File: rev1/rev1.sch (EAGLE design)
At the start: 26 parts, among them IC1 ATMEGA168-AU, Q1 MOSFET-NCHANNEL-IRLR3705ZPBF, Y1 16MHz

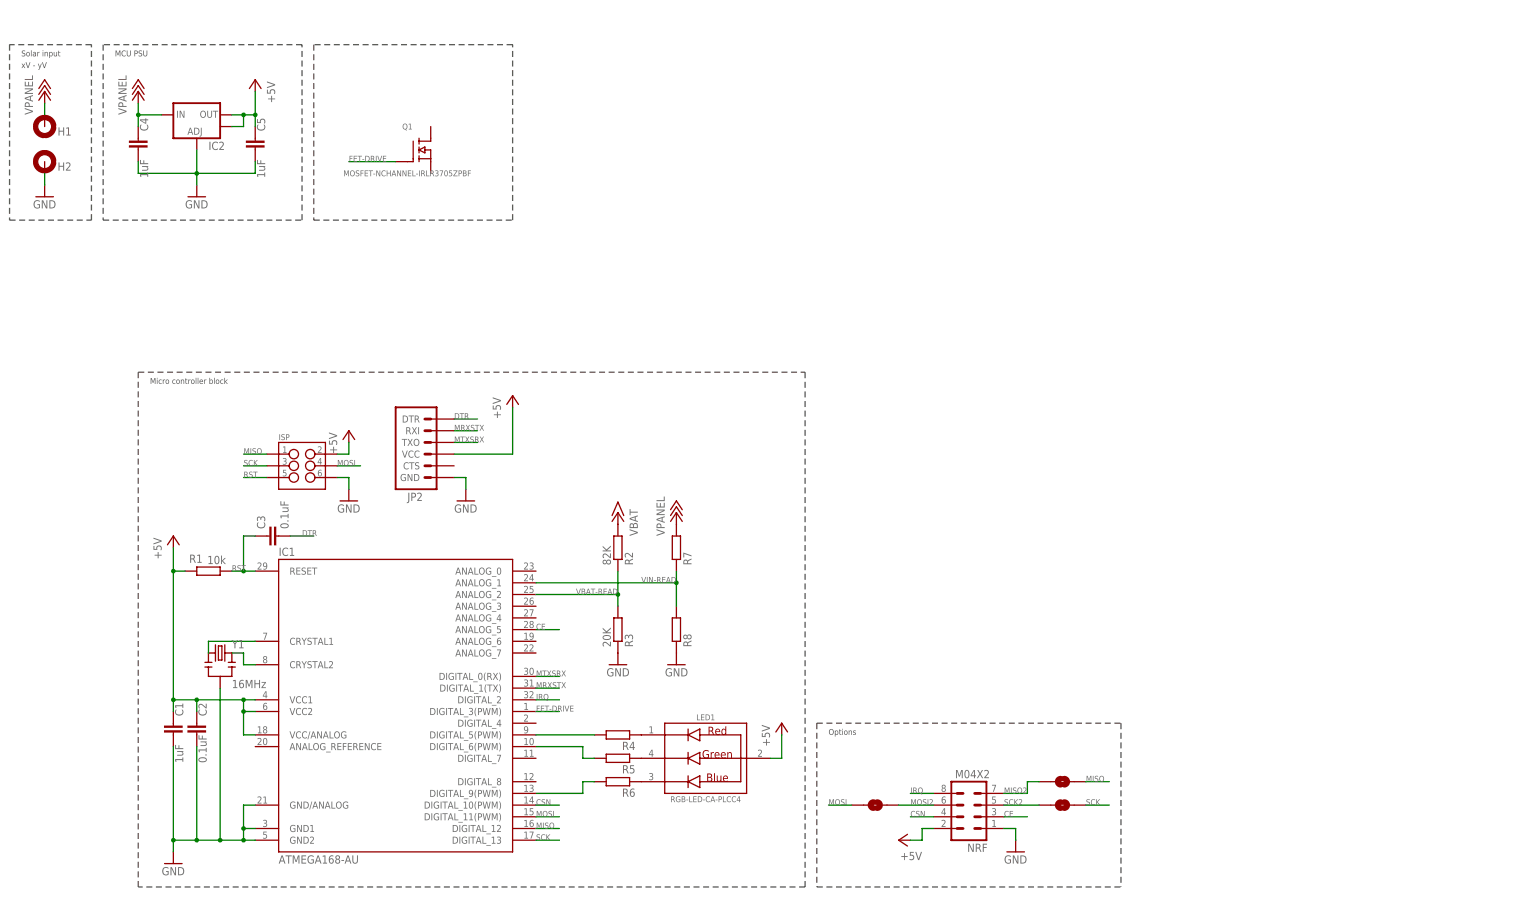
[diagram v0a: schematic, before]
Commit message: Added charge pump for v-gate
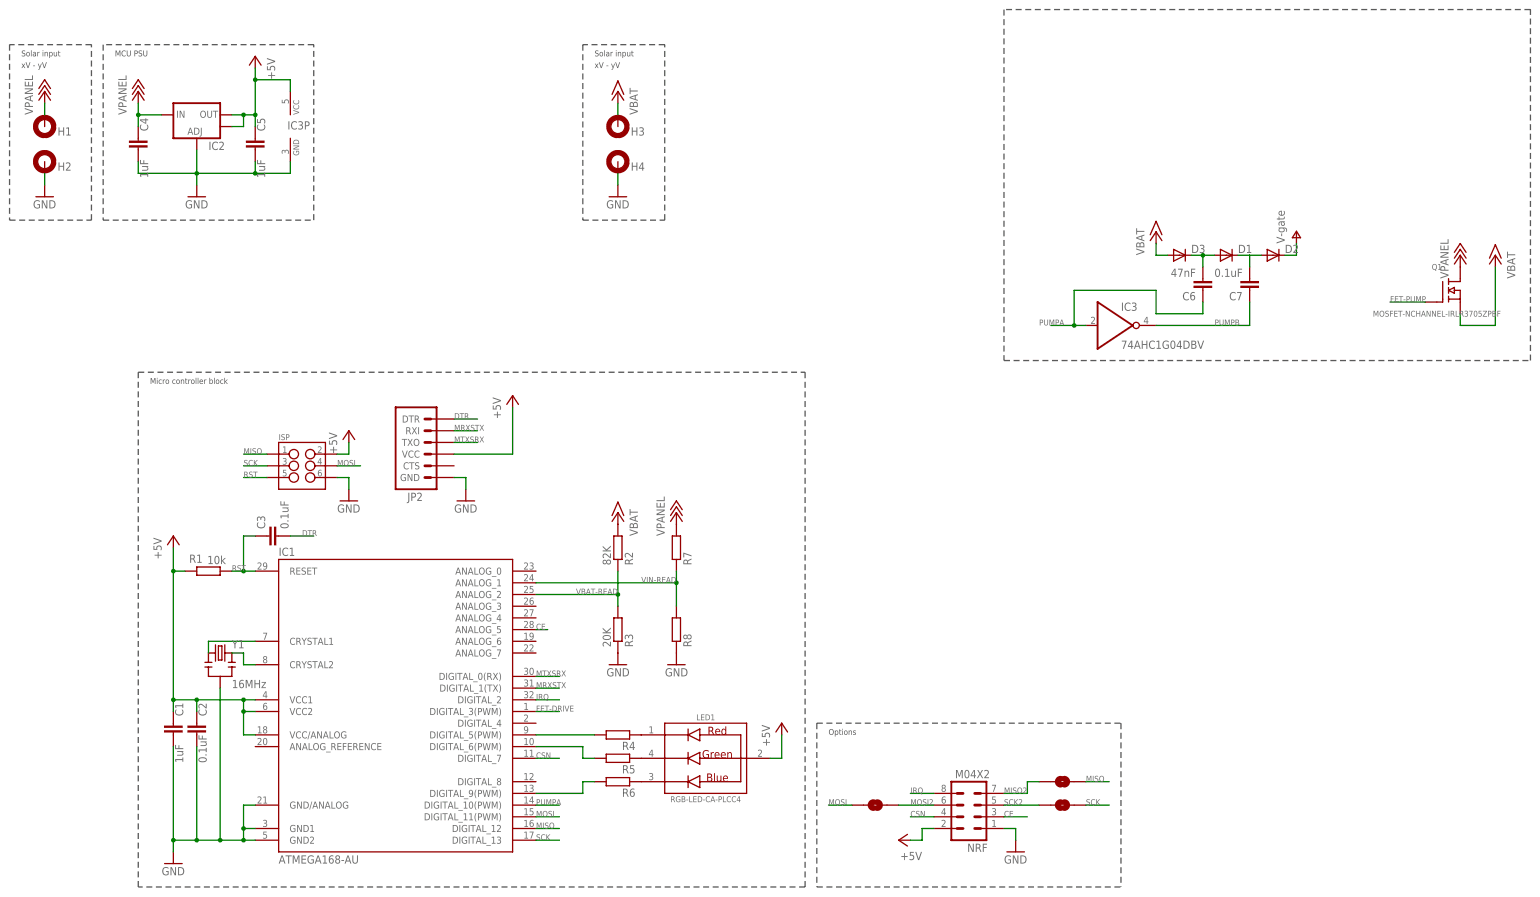
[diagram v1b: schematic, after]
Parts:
- added C6: 47nF, resistor:C-EUC0603K
- added C7: 0.1uF, resistor:C-EUC0603K
- added D1, D2, D3: (no value), SparkFun-DiscreteSemi:DIODESOD
- added H3, H4: MOUNT-PAD-ROUND3.0, holes:MOUNT-PAD-ROUND3.0
- added IC3: 74AHC1G04DBV, 74xx-little-de:74AHC1G04DBV
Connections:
- new net FET-PUMP: Q1.G
- new net N$10: C6.2, D1.A, D3.C
- new net N$8: C7.2, D1.C, D2.A
- new net PUMPA: C6.1, IC1.DIGITAL_10(PWM), IC3A.I
- new net PUMPB: C7.1, IC3A.O
- new net V+: D2.C
- net +15V: now also D3.A, H3.MOUNT, Q1.S
- net +18V: now also Q1.D
- net +5V: now also IC3P.VCC
- net CSN: now also IC1.DIGITAL_7; no longer IC1.DIGITAL_10(PWM)
- net FET-DRIVE: no longer Q1.G
- net GND: now also H4.MOUNT, IC3P.GND
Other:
- moved on the sheet: Q1

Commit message: Schematic pre-finished. Needs values added
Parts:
- added C8: 1uF, resistor:C-EUC0603K
- added Q2: MOSFET-PCHANNELSMD, SparkFun-DiscreteSemi:MOSFET-PCHANNELSMD
- added Q3: MOSFET-NCHANNELBSS138, SparkFun-DiscreteSemi:MOSFET-NCHANNELBSS138
- added R9: 10k, resistor:R-EU_R0603
- C7: value 0.1uF -> 47nF
- D1, D2, D3: value (none) -> DIODE-SCHOTTKY; device SparkFun-DiscreteSemi:DIODESOD -> SparkFun-DiscreteSemi:DIODE-SCHOTTKY
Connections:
- new net N$28: Q2.D, Q3.D
- net +15V: now also R9.1
- net FET-DRIVE: now also Q2.G, Q3.G
- net FET-PUMP: now also R9.2
- net GND: now also C8.1, Q3.S
- net V+: now also C8.2, Q2.S
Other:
- note added: "Battery output"
- note added: "Charge pump"
- note added: "Fet-drive"
- moved on the sheet: C4, C5, C6, C7, H1, H2, H3, H4, IC2, IC3, IC3P, Q1

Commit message: Board laid out
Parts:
- IC2: value (none) -> 5v
- Q2: value MOSFET-PCHANNELSMD -> MOSFET-PCHANNEL; device SparkFun-DiscreteSemi:MOSFET-PCHANNELSMD -> SparkFun-DiscreteSemi:MOSFET-PCHANNEL
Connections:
- removed net N$28: Q2.D, Q3.D
- net FET-PUMP: now also Q2.D, Q3.D
- net VBAT-READ: now also IC1.ANALOG_1; no longer IC1.ANALOG_2
- net VIN-READ: now also IC1.ANALOG_2; no longer IC1.ANALOG_1
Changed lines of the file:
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@@
 <part name="GND7" library="supply1" deviceset="GND" device=""/>
 <part name="P+8" library="supply1" deviceset="+18V" device="" value="VPANEL"/>
-<part name="IC2" library="SparkFun-PowerIC" deviceset="V_REG_LM1117" device="SOT223"/>
+<part name="IC2" library="SparkFun-PowerIC" deviceset="V_REG_LM1117" device="SOT223" value="5v"/>
 <part name="C4" library="resistor" deviceset="C-EU" device="C0603K" value="1uF"/>
 <part name="GND8" library="supply1" deviceset="GND" device=""/>
@@
 <part name="R9" library="resistor" deviceset="R-EU_" device="R0603" value="10k"/>
 <part name="Q3" library="SparkFun-DiscreteSemi" deviceset="MOSFET-NCHANNEL" device="BSS138"/>
-<part name="Q2" library="SparkFun-DiscreteSemi" deviceset="MOSFET-PCHANNEL" device="SMD"/>
+<part name="Q2" library="SparkFun-DiscreteSemi" deviceset="MOSFET-PCHANNEL" device="" value="MOSFET-PCHANNEL"/>
 <part name="GND11" library="supply1" deviceset="GND" device=""/>
 <part name="P+16" library="supply1" deviceset="V+" device="" value="V-gate"/>
@@
 <pinref part="R3" gate="G$1" pin="2"/>
 <pinref part="R2" gate="G$1" pin="1"/>
-<wire x1="-27.94" y1="12.7" x2="-27.94" y2="15.24" width="0.1524" layer="91"/>
-<wire x1="-27.94" y1="15.24" x2="-27.94" y2="20.32" width="0.1524" layer="91"/>
-<label x="-27.94" y="15.24" size="1.27" layer="95" rot="MR0"/>
-<junction x="-27.94" y="15.24"/>
-<pinref part="IC1" gate="1" pin="ANALOG_2"/>
-<wire x1="-45.72" y1="15.24" x2="-27.94" y2="15.24" width="0.1524" layer="91"/>
+<wire x1="-27.94" y1="12.7" x2="-27.94" y2="17.78" width="0.1524" layer="91"/>
+<wire x1="-27.94" y1="17.78" x2="-27.94" y2="20.32" width="0.1524" layer="91"/>
+<label x="-27.94" y="17.78" size="1.27" layer="95" rot="MR0"/>
+<junction x="-27.94" y="17.78"/>
+<wire x1="-45.72" y1="17.78" x2="-27.94" y2="17.78" width="0.1524" layer="91"/>
+<pinref part="IC1" gate="1" pin="ANALOG_1"/>
 </segment>
 </net>
@@
 <pinref part="R8" gate="G$1" pin="2"/>
 <pinref part="R7" gate="G$1" pin="1"/>
-<wire x1="-15.24" y1="12.7" x2="-15.24" y2="17.78" width="0.1524" layer="91"/>
-<label x="-15.24" y="17.78" size="1.27" layer="95" rot="MR0"/>
-<wire x1="-15.24" y1="17.78" x2="-15.24" y2="20.32" width="0.1524" layer="91"/>
-<junction x="-15.24" y="17.78"/>
-<wire x1="-15.24" y1="17.78" x2="-45.72" y2="17.78" width="0.1524" layer="91"/>
-<pinref part="IC1" gate="1" pin="ANALOG_1"/>
+<wire x1="-15.24" y1="12.7" x2="-15.24" y2="15.24" width="0.1524" layer="91"/>
+<label x="-15.24" y="15.24" size="1.27" layer="95" rot="MR0"/>
+<wire x1="-15.24" y1="15.24" x2="-15.24" y2="20.32" width="0.1524" layer="91"/>
+<junction x="-15.24" y="15.24"/>
+<wire x1="-15.24" y1="15.24" x2="-45.72" y2="15.24" width="0.1524" layer="91"/>
+<pinref part="IC1" gate="1" pin="ANALOG_2"/>
 </segment>
 </net>
@@
 <pinref part="R9" gate="G$1" pin="2"/>
 <wire x1="50.8" y1="10.16" x2="50.8" y2="12.7" width="0.1524" layer="91"/>
-<wire x1="50.8" y1="12.7" x2="43.18" y2="12.7" width="0.1524" layer="91"/>
 <junction x="50.8" y="12.7"/>
+<wire x1="38.1" y1="12.7" x2="50.8" y2="12.7" width="0.1524" layer="91"/>
+<pinref part="Q3" gate="G$1" pin="D"/>
+<wire x1="38.1" y1="10.16" x2="38.1" y2="12.7" width="0.1524" layer="91"/>
+<pinref part="Q2" gate="G$1" pin="D"/>
+<wire x1="38.1" y1="15.24" x2="38.1" y2="12.7" width="0.1524" layer="91"/>
+<junction x="38.1" y="12.7"/>
 </segment>
 </net>
@@
 <wire x1="-17.78" y1="91.44" x2="-20.32" y2="91.44" width="0.1524" layer="91"/>
 <wire x1="-17.78" y1="88.9" x2="-17.78" y2="91.44" width="0.1524" layer="91"/>
+<junction x="-17.78" y="91.44"/>
 </segment>
 </net>
@@
 </segment>
 </net>
-<net name="N$28" class="0">
-<segment>
-<wire x1="38.1" y1="12.7" x2="43.18" y2="12.7" width="0.1524" layer="91"/>
-<pinref part="Q3" gate="G$1" pin="D"/>
-<wire x1="38.1" y1="10.16" x2="38.1" y2="12.7" width="0.1524" layer="91"/>
-<pinref part="Q2" gate="G$1" pin="D"/>
-<wire x1="38.1" y1="15.24" x2="38.1" y2="12.7" width="0.1524" layer="91"/>
-<junction x="38.1" y="12.7"/>
-</segment>
-</net>
 </nets>
 </sheet>
 </sheets>
+<errors>
+</errors>
 </schematic>
 </drawing>

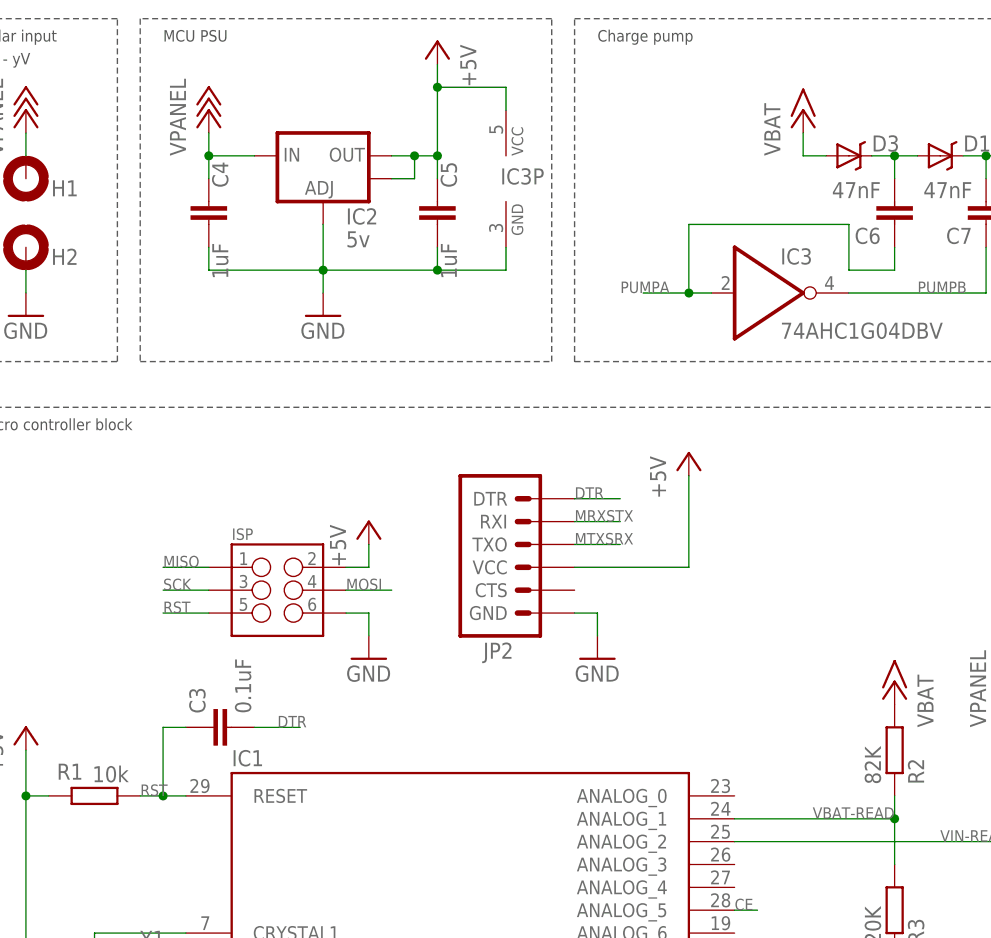
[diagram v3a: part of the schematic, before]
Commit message: Fixing LDO input pin
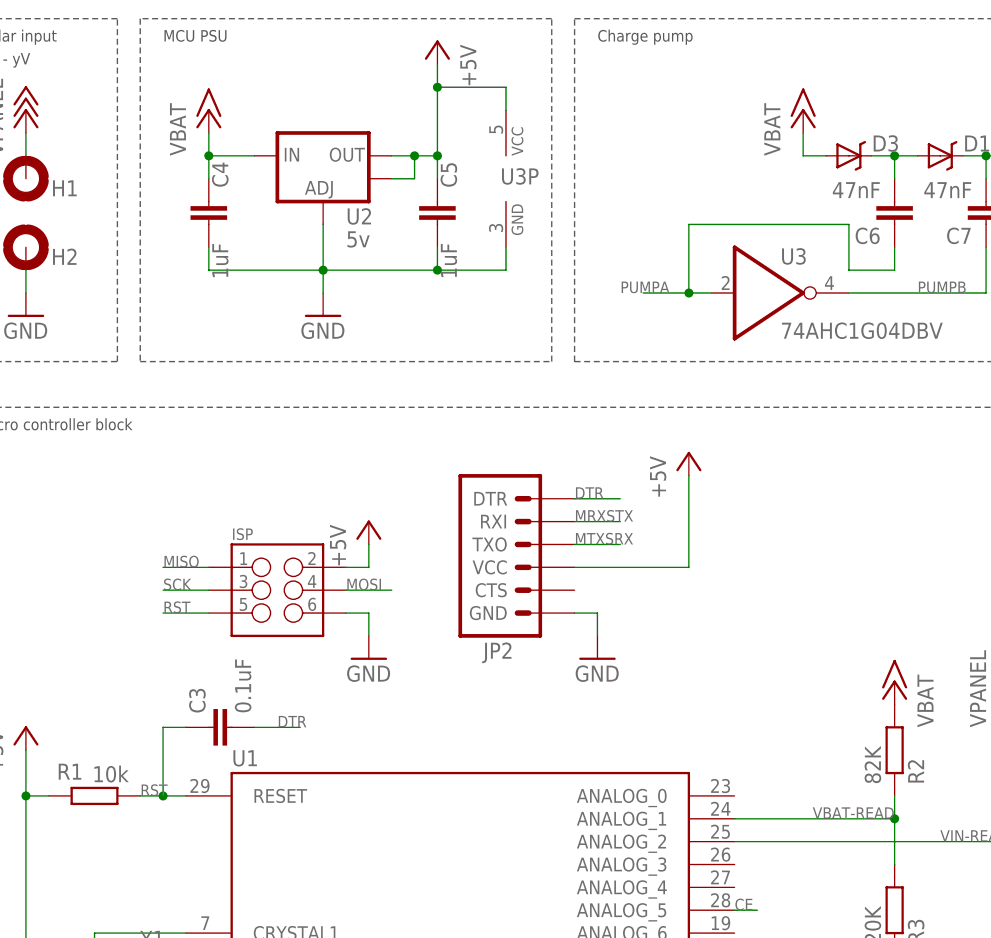
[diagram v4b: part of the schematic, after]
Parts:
- renumbered IC1 to U1, IC2 to U2, IC3 to U3
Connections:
- net +15V: now also C4.1, U2.IN
- net +18V: no longer C4.1, U2.IN
